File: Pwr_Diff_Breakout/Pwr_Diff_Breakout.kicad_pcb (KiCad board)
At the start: 2 copper layers, 60.2 x 85.1 mm, 19 parts, among them J1 RJ45, J2 RJ45, J3 RJ45, J4 RJ45, J5 RJ45

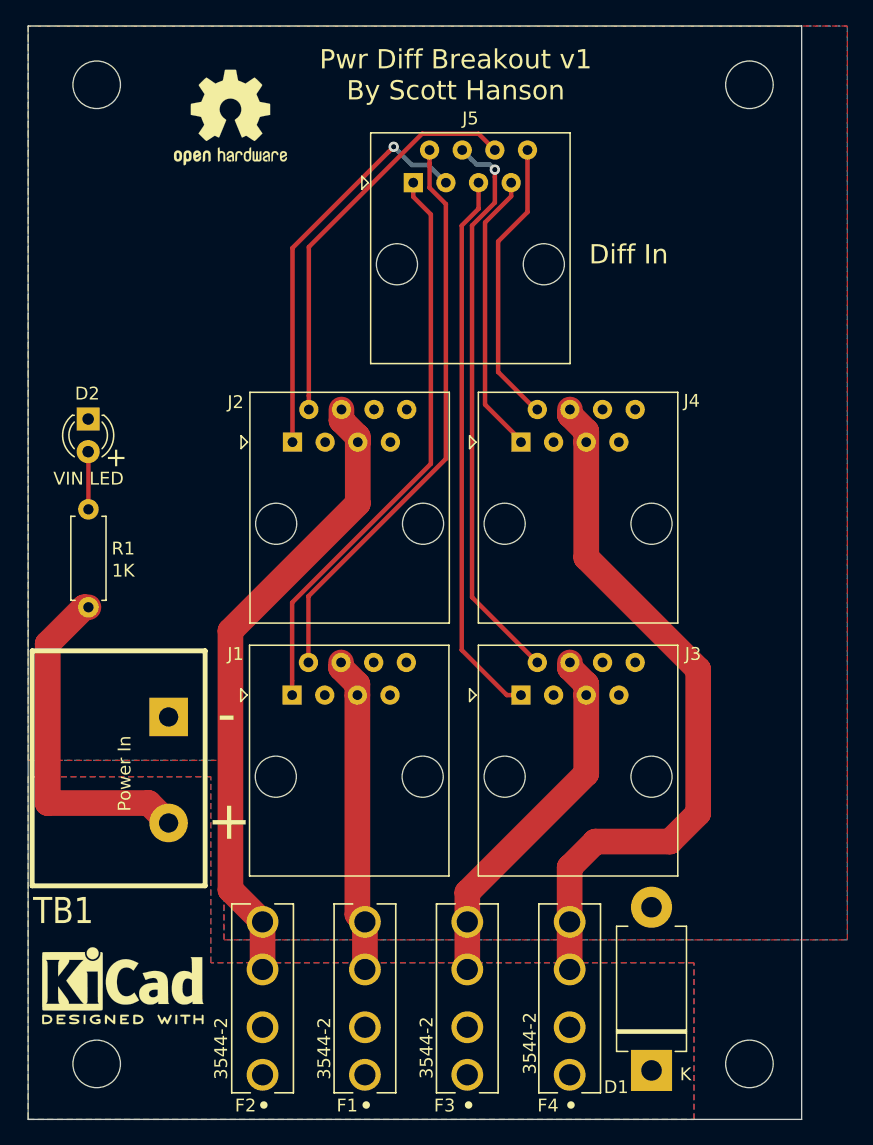
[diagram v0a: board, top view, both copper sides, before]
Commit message: Added some pdf schematics increased Pwr Diff Breakout header spacing
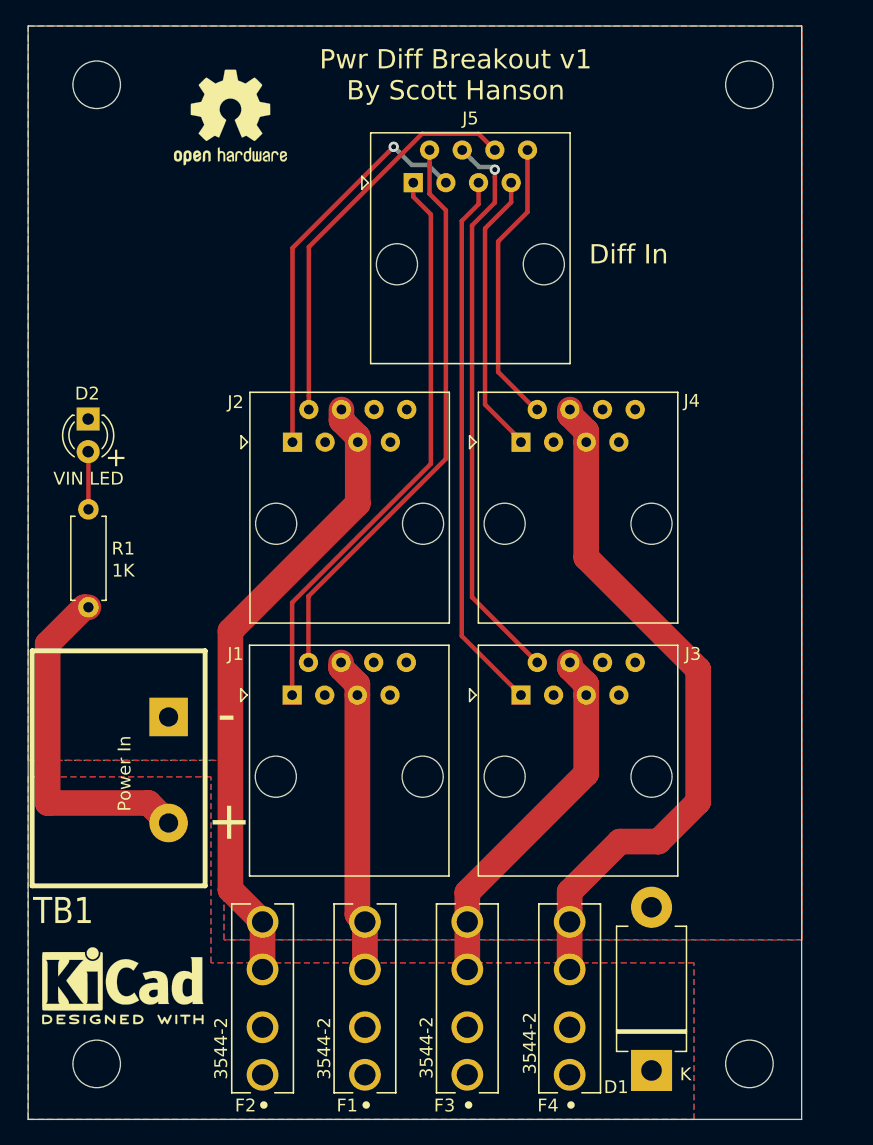
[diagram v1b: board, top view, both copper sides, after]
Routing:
- net VOUT4: track 55.2 -> 53.6 mm
- net Net-(J3-Pad1): track 43.0 -> 42.3 mm
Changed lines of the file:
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@@
   )
   (layers
-    (0 F.Cu signal hide)
-    (31 B.Cu signal hide)
+    (0 F.Cu signal)
+    (31 B.Cu signal)
     (32 B.Adhes user)
     (33 F.Adhes user)
@@
   (segment (start 114.791 100.182802) (end 113.521 98.912802) (width 2) (layer F.Cu) (net 7))
   (segment (start 114.791 101.0328) (end 114.791 100.182802) (width 2) (layer F.Cu) (net 7))
+  (segment (start 113.501 142.0678) (end 113.501 138.3678) (width 2) (layer F.Cu) (net 7))
   (segment (start 114.791 110.0078) (end 114.791 101.0328) (width 2) (layer F.Cu) (net 7))
   (segment (start 123.501 118.7178) (end 114.791 110.0078) (width 2) (layer F.Cu) (net 7))
-  (segment (start 115.501 132.1178) (end 121.301 132.1178) (width 2) (layer F.Cu) (net 7))
-  (segment (start 113.501 138.3678) (end 113.501 134.1178) (width 2) (layer F.Cu) (net 7))
-  (segment (start 121.301 132.1178) (end 123.501 129.9178) (width 2) (layer F.Cu) (net 7))
-  (segment (start 113.501 134.1178) (end 115.501 132.1178) (width 2) (layer F.Cu) (net 7))
-  (segment (start 123.501 129.9178) (end 123.501 118.7178) (width 2) (layer F.Cu) (net 7))
-  (segment (start 113.501 142.0678) (end 113.501 138.3678) (width 2) (layer F.Cu) (net 7))
+  (segment (start 113.501 136.0178) (end 117.401 132.1178) (width 2) (layer F.Cu) (net 7))
+  (segment (start 113.501 138.3678) (end 113.501 136.0178) (width 2) (layer F.Cu) (net 7))
+  (segment (start 117.401 132.1178) (end 120.401 132.1178) (width 2) (layer F.Cu) (net 7))
+  (segment (start 120.401 132.1178) (end 123.501 129.0178) (width 2) (layer F.Cu) (net 7))
+  (segment (start 123.501 129.0178) (end 123.501 118.7178) (width 2) (layer F.Cu) (net 7))
+  (segment (start 93.171 118.1778) (end 93.171 113.025632) (width 0.35) (layer F.Cu) (net 10))
   (segment (start 102.599 79.36046) (end 102.599 78.2998) (width 0.35) (layer F.Cu) (net 10))
-  (segment (start 93.171 118.1778) (end 93.171 113.025632) (width 0.35) (layer F.Cu) (net 10))
-  (segment (start 102.599 81.234802) (end 102.599 79.36046) (width 0.35) (layer F.Cu) (net 10))
-  (segment (start 103.869 102.327632) (end 103.869 82.504802) (width 0.35) (layer F.Cu) (net 10))
+  (segment (start 103.869 102.327632) (end 103.869 82.9858) (width 0.35) (layer F.Cu) (net 10))
   (segment (start 93.171 113.025632) (end 103.869 102.327632) (width 0.35) (layer F.Cu) (net 10))
-  (segment (start 103.869 82.504802) (end 102.599 81.234802) (width 0.35) (layer F.Cu) (net 10))
+  (segment (start 102.599 81.7158) (end 102.599 79.36046) (width 0.35) (layer F.Cu) (net 10))
+  (segment (start 103.869 82.9858) (end 102.599 81.7158) (width 0.35) (layer F.Cu) (net 10))
   (segment (start 91.901 119.6178) (end 91.901 120.7178) (width 0.35) (layer F.Cu) (net 11))
   (segment (start 101.329 80.8398) (end 101.329 81.9398) (width 0.35) (layer F.Cu) (net 11))
@@
   (segment (start 101.220995 79.461795) (end 100.204999 78.445799) (width 0.35) (layer B.Cu) (net 15))
   (via (at 107.679 79.8238) (size 0.8) (drill 0.4) (layers F.Cu B.Cu) (net 18))
-  (segment (start 105.888999 79.049799) (end 105.139 78.2998) (width 0.35) (layer B.Cu) (net 18))
-  (segment (start 106.263001 79.423801) (end 105.888999 79.049799) (width 0.35) (layer B.Cu) (net 18))
-  (segment (start 107.279001 79.423801) (end 106.263001 79.423801) (width 0.35) (layer B.Cu) (net 18))
-  (segment (start 107.679 79.8238) (end 107.279001 79.423801) (width 0.35) (layer B.Cu) (net 18))
   (segment (start 105.901 113.0978) (end 105.901 84.170628) (width 0.35) (layer F.Cu) (net 18))
   (segment (start 105.901 84.170628) (end 107.679 82.392628) (width 0.35) (layer F.Cu) (net 18))
@@
   (segment (start 107.679 80.389485) (end 107.679 79.8238) (width 0.35) (layer F.Cu) (net 18))
   (segment (start 107.679 82.392628) (end 107.679 80.389485) (width 0.35) (layer F.Cu) (net 18))
-  (segment (start 105.101 117.2078) (end 108.611 120.7178) (width 0.35) (layer F.Cu) (net 19))
-  (segment (start 108.611 120.7178) (end 109.711 120.7178) (width 0.35) (layer F.Cu) (net 19))
-  (segment (start 105.101 84.1798) (end 105.101 117.2078) (width 0.35) (layer F.Cu) (net 19))
-  (segment (start 106.409 80.8398) (end 106.409 82.8718) (width 0.35) (layer F.Cu) (net 19))
-  (segment (start 106.409 82.8718) (end 105.101 84.1798) (width 0.35) (layer F.Cu) (net 19))
+  (segment (start 105.888999 79.049799) (end 105.139 78.2998) (width 0.35) (layer B.Cu) (net 18))
+  (segment (start 106.457 79.6178) (end 105.888999 79.049799) (width 0.35) (layer B.Cu) (net 18))
+  (segment (start 107.679 79.8238) (end 107.473 79.6178) (width 0.35) (layer B.Cu) (net 18))
+  (segment (start 107.473 79.6178) (end 106.457 79.6178) (width 0.35) (layer B.Cu) (net 18))
+  (segment (start 109.701 120.7178) (end 109.711 120.7178) (width 0.35) (layer F.Cu) (net 19))
+  (segment (start 105.101 116.1178) (end 109.701 120.7178) (width 0.35) (layer F.Cu) (net 19))
+  (segment (start 105.101 83.8178) (end 105.101 116.1178) (width 0.35) (layer F.Cu) (net 19))
+  (segment (start 106.409 80.8398) (end 106.409 82.5098) (width 0.35) (layer F.Cu) (net 19))
+  (segment (start 106.409 82.5098) (end 105.101 83.8178) (width 0.35) (layer F.Cu) (net 19))
   (segment (start 110.219 83.1258) (end 110.219 78.2998) (width 0.35) (layer F.Cu) (net 22))
   (segment (start 107.933 85.4118) (end 110.219 83.1258) (width 0.35) (layer F.Cu) (net 22))
@@
   (segment (start 110.981 98.4928) (end 110.854 98.4928) (width 0.35) (layer F.Cu) (net 22))
   (segment (start 110.854 98.4928) (end 107.933 95.5718) (width 0.35) (layer F.Cu) (net 22))
-  (segment (start 106.917 83.93246) (end 106.917 98.1118) (width 0.35) (layer F.Cu) (net 23))
+  (segment (start 106.917 98.1118) (end 109.711 100.9058) (width 0.35) (layer F.Cu) (net 23))
   (segment (start 109.711 100.9058) (end 109.711 101.0328) (width 0.35) (layer F.Cu) (net 23))
-  (segment (start 106.917 98.1118) (end 109.711 100.9058) (width 0.35) (layer F.Cu) (net 23))
-  (segment (start 108.949 80.8398) (end 108.949 81.90046) (width 0.35) (layer F.Cu) (net 23))
-  (segment (start 108.949 81.90046) (end 106.917 83.93246) (width 0.35) (layer F.Cu) (net 23))
+  (segment (start 108.949 80.8398) (end 108.949 82.3698) (width 0.35) (layer F.Cu) (net 23))
+  (segment (start 106.917 84.4018) (end 106.917 98.1118) (width 0.35) (layer F.Cu) (net 23))
+  (segment (start 108.949 82.3698) (end 106.917 84.4018) (width 0.35) (layer F.Cu) (net 23))
   (zone (net 2) (net_name VIN1) (layer F.Cu) (hatch edge 0.508)
     (connect_pads (clearance 0.2))
@@
     (polygon
       (pts
-        (xy 71.357 68.6478) (xy 135.111 68.6478) (xy 135.111 139.7678) (xy 86.597 139.7678) (xy 86.597 125.7978)
+        (xy 71.357 68.6478) (xy 131.601 68.6478) (xy 131.601 139.7678) (xy 86.597 139.7678) (xy 86.597 125.7978)
         (xy 71.357 125.7978)
       )
@@
     (polygon
       (pts
-        (xy 71.357 68.6478) (xy 71.357 125.7978) (xy 86.597 125.7978) (xy 86.597 139.7678) (xy 135.111 139.7678)
-        (xy 135.111 68.6478)
+        (xy 71.357 68.6478) (xy 71.357 125.7978) (xy 86.597 125.7978) (xy 86.597 139.7678) (xy 131.601 139.7778)
+        (xy 131.601 68.6578)
       )
     )

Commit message: update to kicad v9
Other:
- net class 3.3v removed
- net class 5v removed
- net class Default removed
- net class Gnd removed
- net class Power removed
- net class Vin removed
- net class power2 removed
